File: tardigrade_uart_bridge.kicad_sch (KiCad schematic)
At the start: 5 parts, among them J1 Conn_01x08_Socket, J2 Conn_01x03_Socket, J3 Conn_01x02_Socket, J4 Conn_01x02_Socket, J5 Conn_01x05_Socket

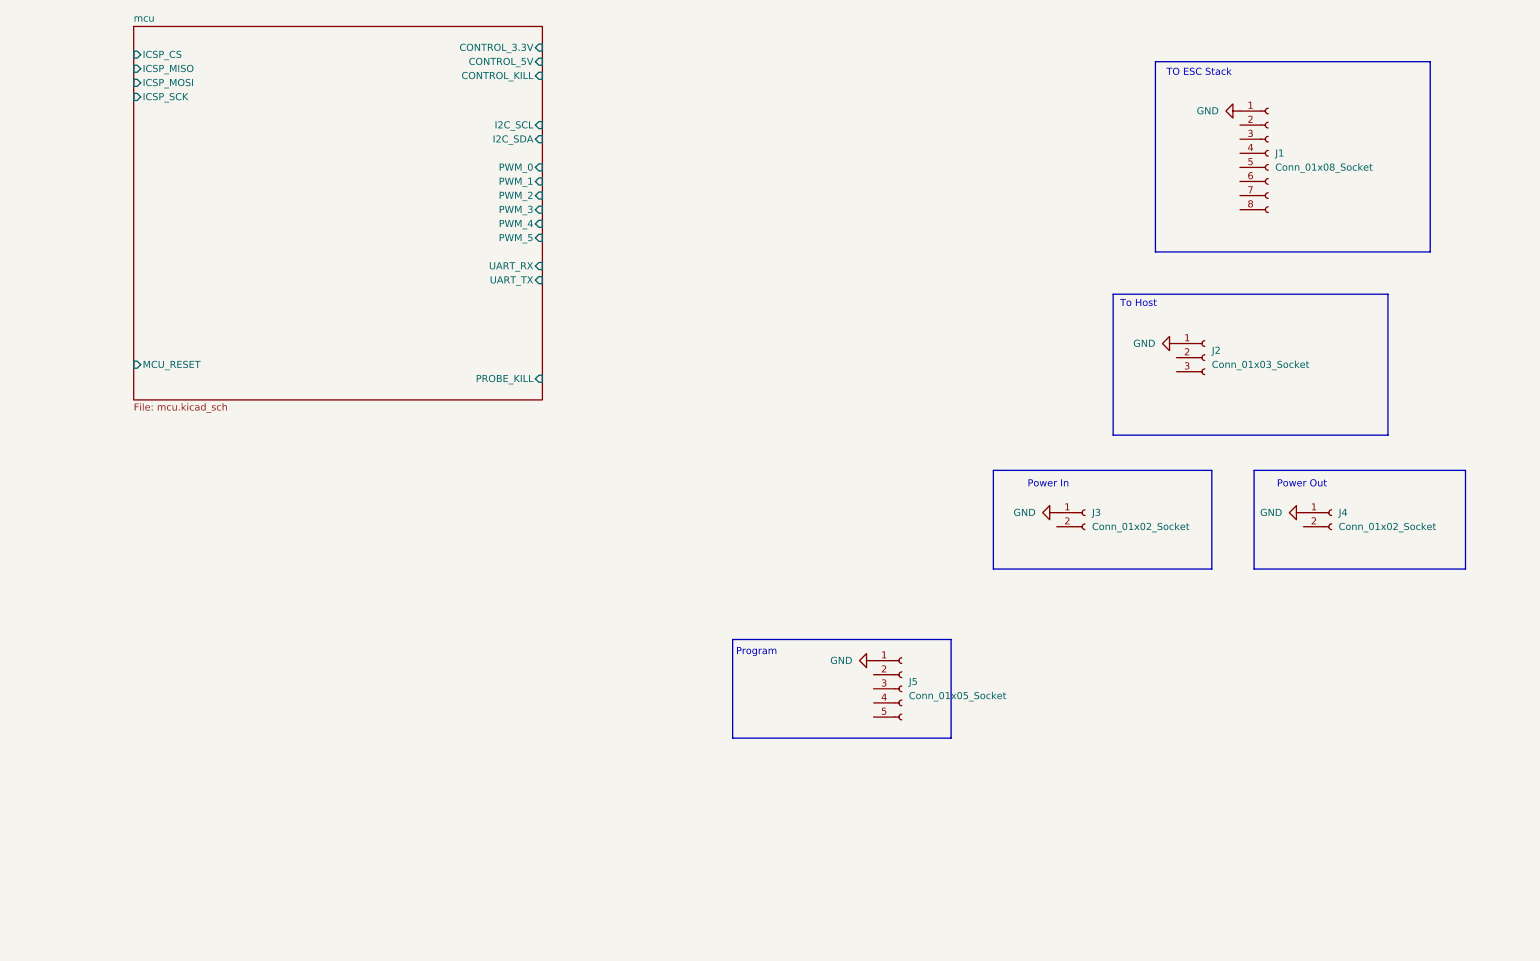
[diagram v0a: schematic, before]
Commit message: added LDO, a few other things
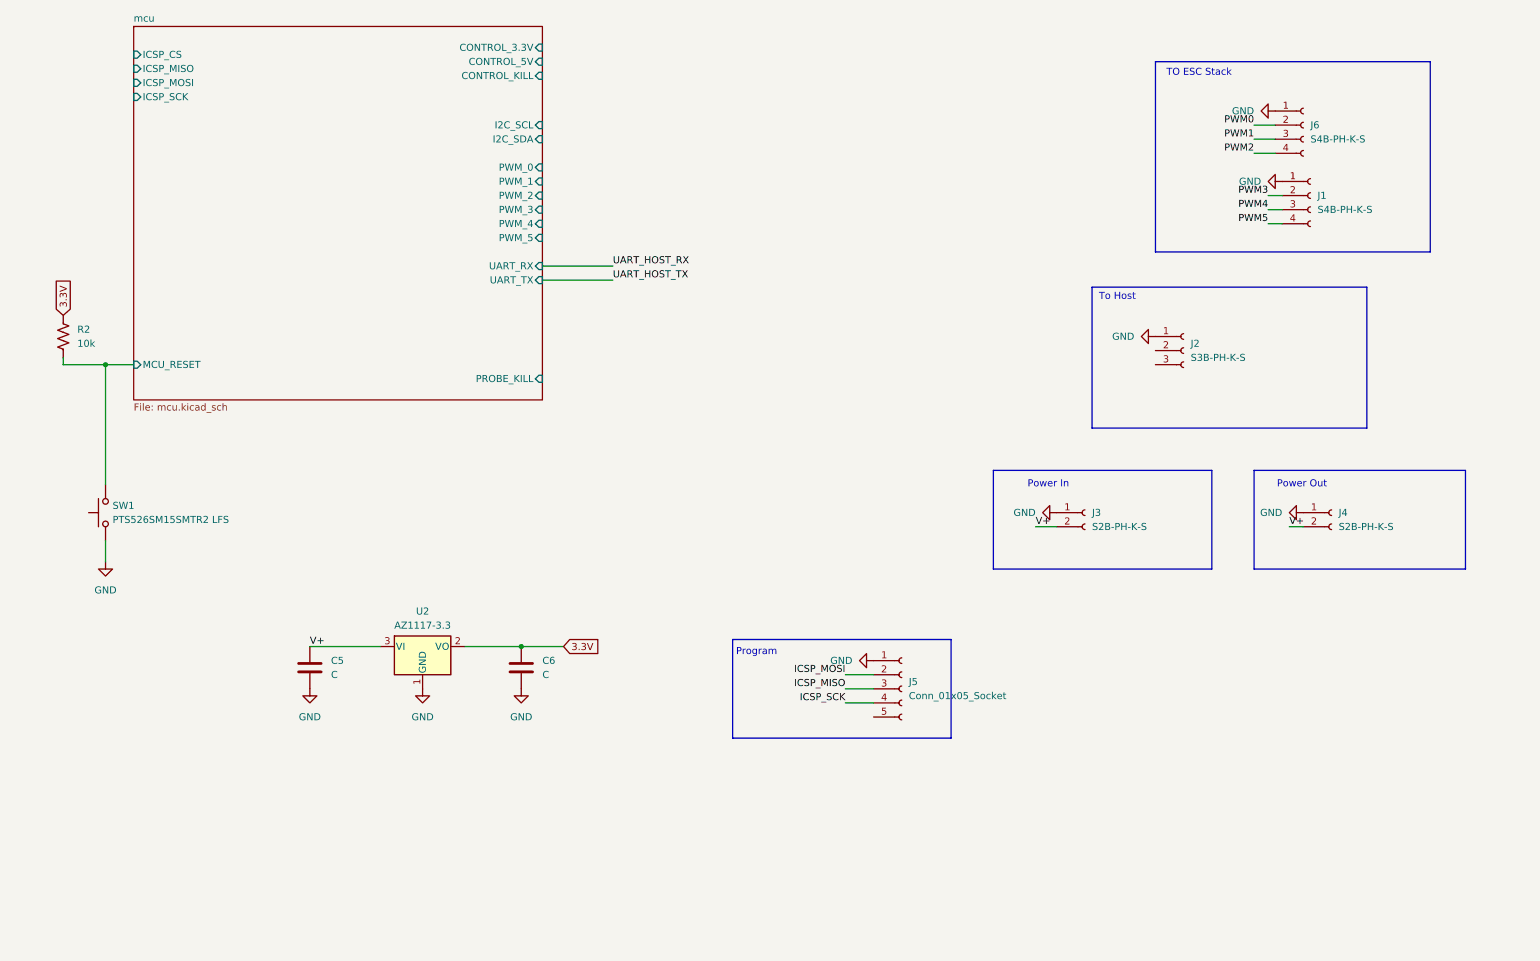
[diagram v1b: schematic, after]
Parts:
- removed J1: Conn_01x08_Socket, symbol Connector:Conn_01x08_Socket
- added C5, C6: C, symbol Device:C
- added J1, J6: S4B-PH-K-S, Connector_JST:JST_PH_S4B-PH-K_1x04_P2.00mm_Horizontal, symbol Connector:Conn_01x04_Socket
- added R2: 10k, symbol Device:R_US
- added SW1: PTS526SM15SMTR2 LFS, symbol Switch:SW_Push
- added U2: AZ1117-3.3, Package_TO_SOT_SMD:SOT-223-3_TabPin2, symbol Regulator_Linear:AZ1117-3.3
- J2: value Conn_01x03_Socket -> S3B-PH-K-S
- J3, J4: value Conn_01x02_Socket -> S2B-PH-K-S
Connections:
- net GND: now also C5.2, C6.2, J1.1 (Pin_1), J6.1 (Pin_1), SW1.1, U2.1 (GND)
- net mcu/MCU_RESET: now also R2.1, SW1.2
- net V+: now reaches J4.2 (Pin_2)
- net V+: now also J3.2 (Pin_2), C5.1, U2.3 (VI)
- net ICSP_MOSI: now reaches J5.2 (Pin_2)
- net ICSP_MISO: now reaches J5.3 (Pin_3)
- net ICSP_SCK: now reaches J5.4 (Pin_4)
- new net 3.3V: C6.1, R2.2, U2.2 (VO)
- new net PWM0: J6.2 (Pin_2)
- new net PWM1: J6.3 (Pin_3)
- new net PWM2: J6.4 (Pin_4)
- new net PWM3: J1.2 (Pin_2)
- new net PWM4: J1.3 (Pin_3)
- new net PWM5: J1.4 (Pin_4)
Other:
- moved on the sheet: J2

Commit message: added peripheral connectors, started PCB
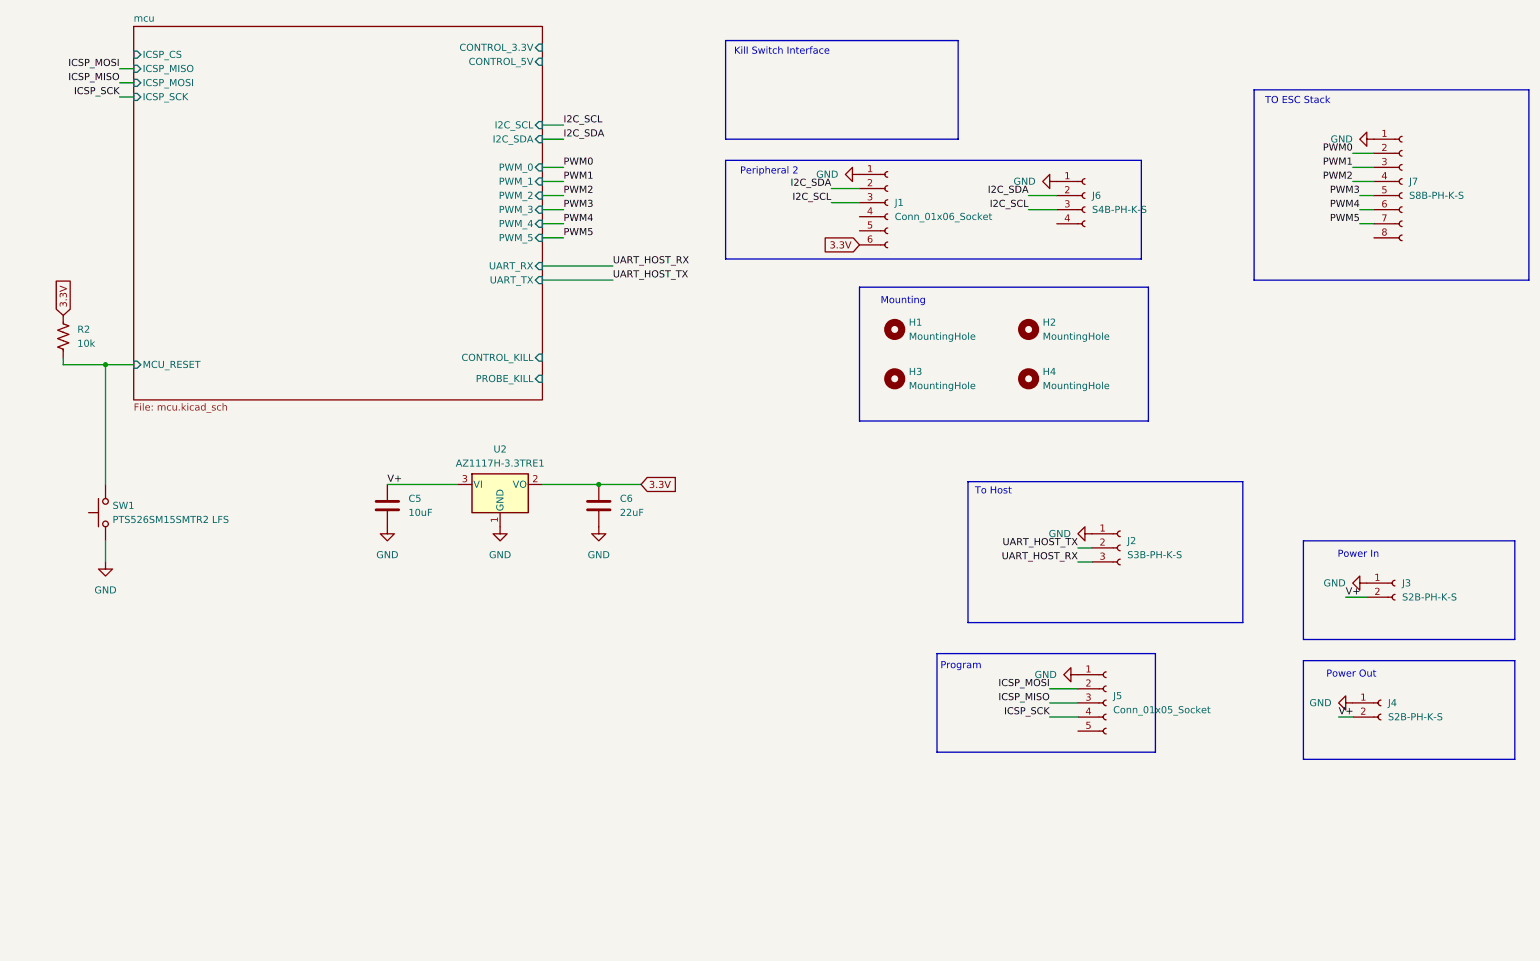
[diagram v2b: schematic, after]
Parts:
- removed J1: S4B-PH-K-S, Connector_JST:JST_PH_S4B-PH-K_1x04_P2.00mm_Horizontal, symbol Connector:Conn_01x04_Socket
- added H1, H2, H3, H4: MountingHole, MountingHole:MountingHole_3.2mm_M3, symbol Mechanical:MountingHole
- added J1: Conn_01x06_Socket, Connector_PinHeader_2.54mm:PinHeader_1x06_P2.54mm_Vertical, symbol Connector:Conn_01x06_Socket
- added J7: S8B-PH-K-S, Connector_JST:JST_PH_S8B-PH-K_1x08_P2.00mm_Horizontal, symbol Connector:Conn_01x08_Socket
- C5: value C -> 10uF; footprint (none) -> Capacitor_SMD:C_0805_2012Metric_Pad1.18x1.45mm_HandSolder
- C6: value C -> 22uF; footprint (none) -> Capacitor_SMD:C_0805_2012Metric_Pad1.18x1.45mm_HandSolder
- J5: footprint (none) -> Connector_PinHeader_2.54mm:PinHeader_1x05_P2.54mm_Vertical
- J6: footprint Connector_JST:JST_PH_S4B-PH-K_1x04_P2.00mm_Horizontal -> Connector_JST:JST_PH_B4B-PH-K_1x04_P2.00mm_Vertical
- R2: footprint (none) -> Capacitor_SMD:C_0805_2012Metric_Pad1.18x1.45mm_HandSolder
- U2: value AZ1117-3.3 -> AZ1117H-3.3TRE1
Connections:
- net 3.3V: now also J1.6 (Pin_6)
- net GND: now also J1.1 (Pin_1), J7.1 (Pin_1)
- net PWM0: now also J7.2 (Pin_2); no longer J6.2 (Pin_2)
- net PWM1: now also J7.3 (Pin_3); no longer J6.3 (Pin_3)
- net PWM2: now also J7.4 (Pin_4); no longer J6.4 (Pin_4)
- net PWM3: now also J7.5 (Pin_5)
- net PWM4: now also J7.6 (Pin_6)
- net PWM5: now also J7.7 (Pin_7)
- net UART_HOST_RX: now also J2.3 (Pin_3)
- net UART_HOST_TX: now also J2.2 (Pin_2)
- new net I2C_SCL: J1.3 (Pin_3), J6.3 (Pin_3)
- new net I2C_SDA: J1.2 (Pin_2), J6.2 (Pin_2)
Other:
- note added: "Kill Switch Interface"
- note added: "Mounting"
- note added: "Peripheral 2"
- moved on the sheet: C5, C6, J2, J3, J4, J5, U2

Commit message: added pwm outputs, power connectors, etc.
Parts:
- removed J2: S3B-PH-K-S, symbol Connector:Conn_01x03_Socket
- added D1, D2: LED_TX, LED_SMD:LED_0805_2012Metric_Pad1.15x1.40mm_HandSolder, symbol Device:LED
- added D3: LED_PWR, LED_SMD:LED_0805_2012Metric_Pad1.15x1.40mm_HandSolder, symbol Device:LED
- added J8: S4B-PH-K-S, Connector_JST:JST_PH_S4B-PH-K_1x04_P2.00mm_Horizontal, symbol Connector:Conn_01x04_Socket
- added Q1, Q2: MMBT2222A-TP, digikey-footprints:SOT-23-3, symbol dk_Transistors-Bipolar-BJT-Single:MMBT2222A-TP
- added R3, R4, R5: 1K, symbol Device:R_US
- J3, J4: footprint (none) -> Connector_JST:JST_PH_S2B-PH-K_1x02_P2.00mm_Horizontal
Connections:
- net 3.3V: now also R5.1; no longer C6.1, U2.2 (VO)
- net GND: now also D3.1 (K), J8.1 (Pin_1), Q1.2 (E), Q2.2 (E)
- net UART_HOST_RX: now also J8.3 (Pin_3), Q2.1 (B)
- net UART_HOST_TX: now also J8.2 (Pin_2), Q1.1 (B)
- net V+: now also J8.4 (Pin_4), R3.1, R4.1
- new net: D1.2 (A), R3.2
- new net: C6.1, U2.2 (VO)
- new net: D3.2 (A), R5.2
- new net: D1.1 (K), Q1.3 (C)
- new net: D2.1 (K), Q2.3 (C)
- new net: D2.2 (A), R4.2
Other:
- note added: "Power 1"
- note added: "Power 2"
- note removed: "Power In"
- note removed: "Power Out"
